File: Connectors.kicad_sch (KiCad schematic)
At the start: 4 parts, among them J1 Screw_Terminal_01x07, J3 Conn_01x05

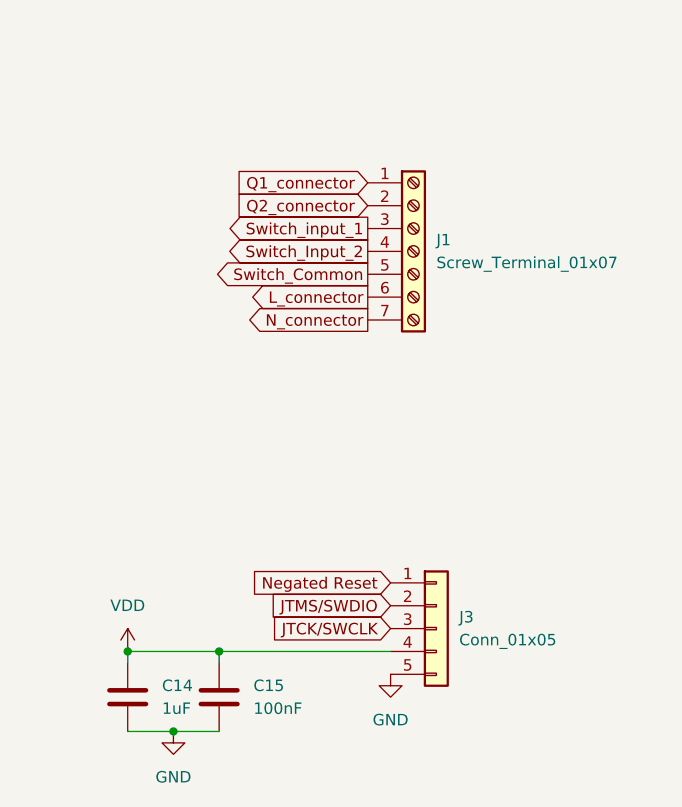
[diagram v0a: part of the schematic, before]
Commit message: Dodanie footprintów
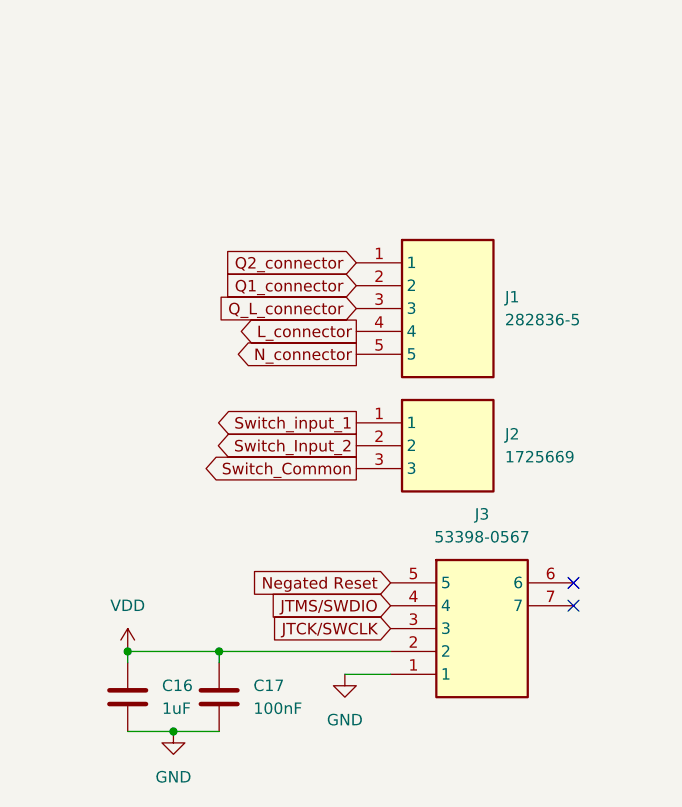
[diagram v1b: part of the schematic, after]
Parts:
- removed J1: Screw_Terminal_01x07, symbol Connector:Screw_Terminal_01x07
- removed J3: Conn_01x05, symbol Connector_Generic:Conn_01x05
- added J1: 282836-5, Sterownik_roletyLibrary:2828365, symbol 282836-5:282836-5
- added J2: 1725669, Sterownik_roletyLibrary:1725669, symbol 1725669:1725669
- added J3: 53398-0567, Sterownik_roletyLibrary:533980567, symbol 53398-0567:53398-0567
- C16: renamed from C14; footprint (none) -> Capacitor_SMD:C_0201_0603Metric
- C17: renamed from C15; footprint (none) -> Capacitor_SMD:C_0201_0603Metric
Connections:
- net GND: now also J3.1
- net JTCK/SWCLK: now also J3.3
- net JTMS/SWDIO: now also J3.4
- net L_connector: now also J1.4
- net N_connector: now also J1.5
- net Negated Reset: now also J3.5
- net Q1_connector: now also J1.2
- net Q2_connector: now also J1.1
- net Switch_Common: now also J2.3
- net Switch_Input_2: now also J2.2
- net Switch_input_1: now also J2.1
- net VDD: now also J3.2
- new net Q_L_connector: J1.3
- no-connect marks 0 -> 2

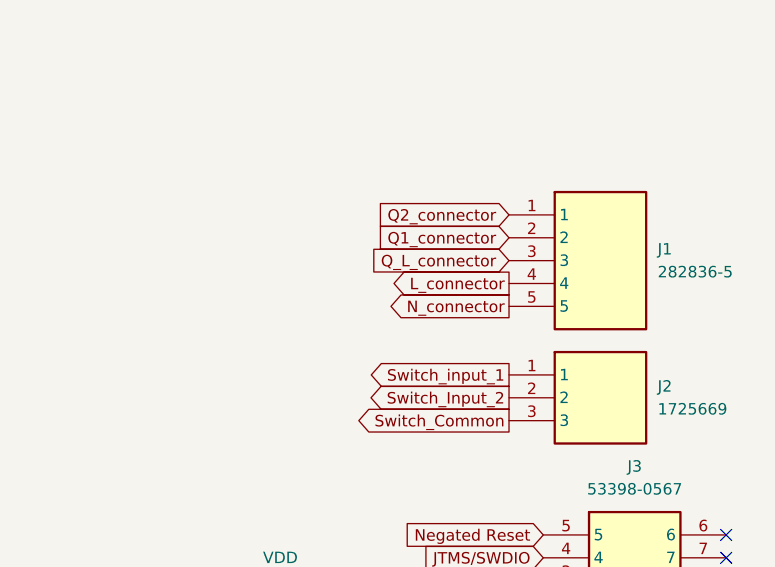
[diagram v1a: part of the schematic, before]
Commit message: początkowe rozłożenie na PCB
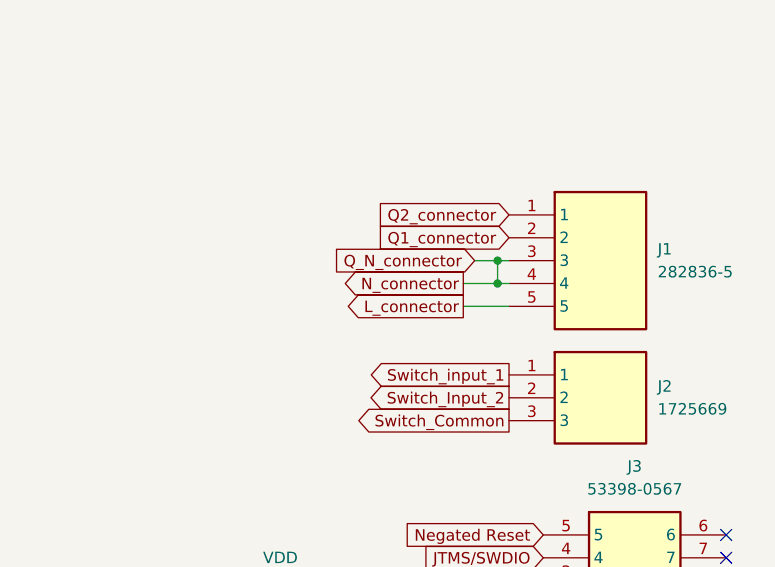
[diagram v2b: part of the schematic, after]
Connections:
- net Q_L_connector is gone; now on net N_connector: J1.3
- net L_connector: now also J1.5; no longer J1.4
- net N_connector: now also J1.4; no longer J1.5
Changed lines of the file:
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@@
+	)
+	(junction
+		(at 96.52 88.9)
+		(diameter 0)
+		(color 0 0 0 0)
 	)
 	(junction
@@
 		(color 0 0 0 0)
 	)
+	(junction
+		(at 96.52 86.36)
+		(diameter 0)
+		(color 0 0 0 0)
+	)
 	(no_connect
 		(at 121.92 119.38)
@@
 	(wire
 		(pts
+			(xy 96.52 88.9) (xy 97.79 88.9)
+		)
+		(stroke
+			(width 0)
+			(type default)
+		)
+	)
+	(wire
+		(pts
 			(xy 82.55 124.46) (xy 82.55 125.73)
 		)
@@
 	(wire
 		(pts
+			(xy 96.52 86.36) (xy 97.79 86.36)
+		)
+		(stroke
+			(width 0)
+			(type default)
+		)
+	)
+	(wire
+		(pts
+			(xy 93.98 86.36) (xy 96.52 86.36)
+		)
+		(stroke
+			(width 0)
+			(type default)
+		)
+	)
+	(wire
+		(pts
+			(xy 92.71 88.9) (xy 96.52 88.9)
+		)
+		(stroke
+			(width 0)
+			(type default)
+		)
+	)
+	(wire
+		(pts
+			(xy 92.71 91.44) (xy 97.79 91.44)
+		)
+		(stroke
+			(width 0)
+			(type default)
+		)
+	)
+	(wire
+		(pts
 			(xy 72.39 133.35) (xy 77.47 133.35)
 		)
@@
 		(pts
 			(xy 101.6 124.46) (xy 82.55 124.46)
+		)
+		(stroke
+			(width 0)
+			(type default)
+		)
+	)
+	(wire
+		(pts
+			(xy 96.52 86.36) (xy 96.52 88.9)
 		)
 		(stroke
@@
 		)
 	)
-	(global_label "L_connector"
+	(global_label "N_connector"
 		(shape output)
-		(at 97.79 88.9 180)
-		(fields_autoplaced yes)
-		(effects
-			(font
-				(size 1.27 1.27)
-			)
-			(justify right)
-		)
-		(property "Intersheetrefs" "${INTERSHEET_REFS}"
-			(at 83.4354 88.9 0)
+		(at 92.71 88.9 180)
+		(fields_autoplaced yes)
+		(effects
+			(font
+				(size 1.27 1.27)
+			)
+			(justify right)
+		)
+		(property "Intersheetrefs" "${INTERSHEET_REFS}"
+			(at 78.053 88.9 0)
 			(effects
 				(font
@@
 		)
 	)
-	(global_label "Q_L_connector"
-		(shape input)
-		(at 97.79 86.36 180)
-		(fields_autoplaced yes)
-		(effects
-			(font
-				(size 1.27 1.27)
-			)
-			(justify right)
-		)
-		(property "Intersheetrefs" "${INTERSHEET_REFS}"
-			(at 81.1373 86.36 0)
+	(global_label "Q_N_connector"
+		(shape input)
+		(at 93.98 86.36 180)
+		(fields_autoplaced yes)
+		(effects
+			(font
+				(size 1.27 1.27)
+			)
+			(justify right)
+		)
+		(property "Intersheetrefs" "${INTERSHEET_REFS}"
+			(at 77.0249 86.36 0)
 			(effects
 				(font
@@
 		)
 	)
-	(global_label "N_connector"
+	(global_label "L_connector"
 		(shape output)
-		(at 97.79 91.44 180)
-		(fields_autoplaced yes)
-		(effects
-			(font
-				(size 1.27 1.27)
-			)
-			(justify right)
-		)
-		(property "Intersheetrefs" "${INTERSHEET_REFS}"
-			(at 83.133 91.44 0)
-			(effects
-				(font
+		(at 92.71 91.44 180)
+		(fields_autoplaced yes)
+		(effects
+			(font
+				(size 1.27 1.27)
+			)
+			(justify right)
+		)
+		(property "Intersheetrefs" "${INTERSHEET_REFS}"
+			(at 78.3554 91.44 0)
+			(effects
+				(font
